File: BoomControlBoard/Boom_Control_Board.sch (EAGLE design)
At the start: 43 parts, among them J1 Servo Header, J2 FTDI Header, J7 455-1750-1-ND, U1 ATMEGA328P_TQFP, U2 3.3V/150mA, Y1 16MHz

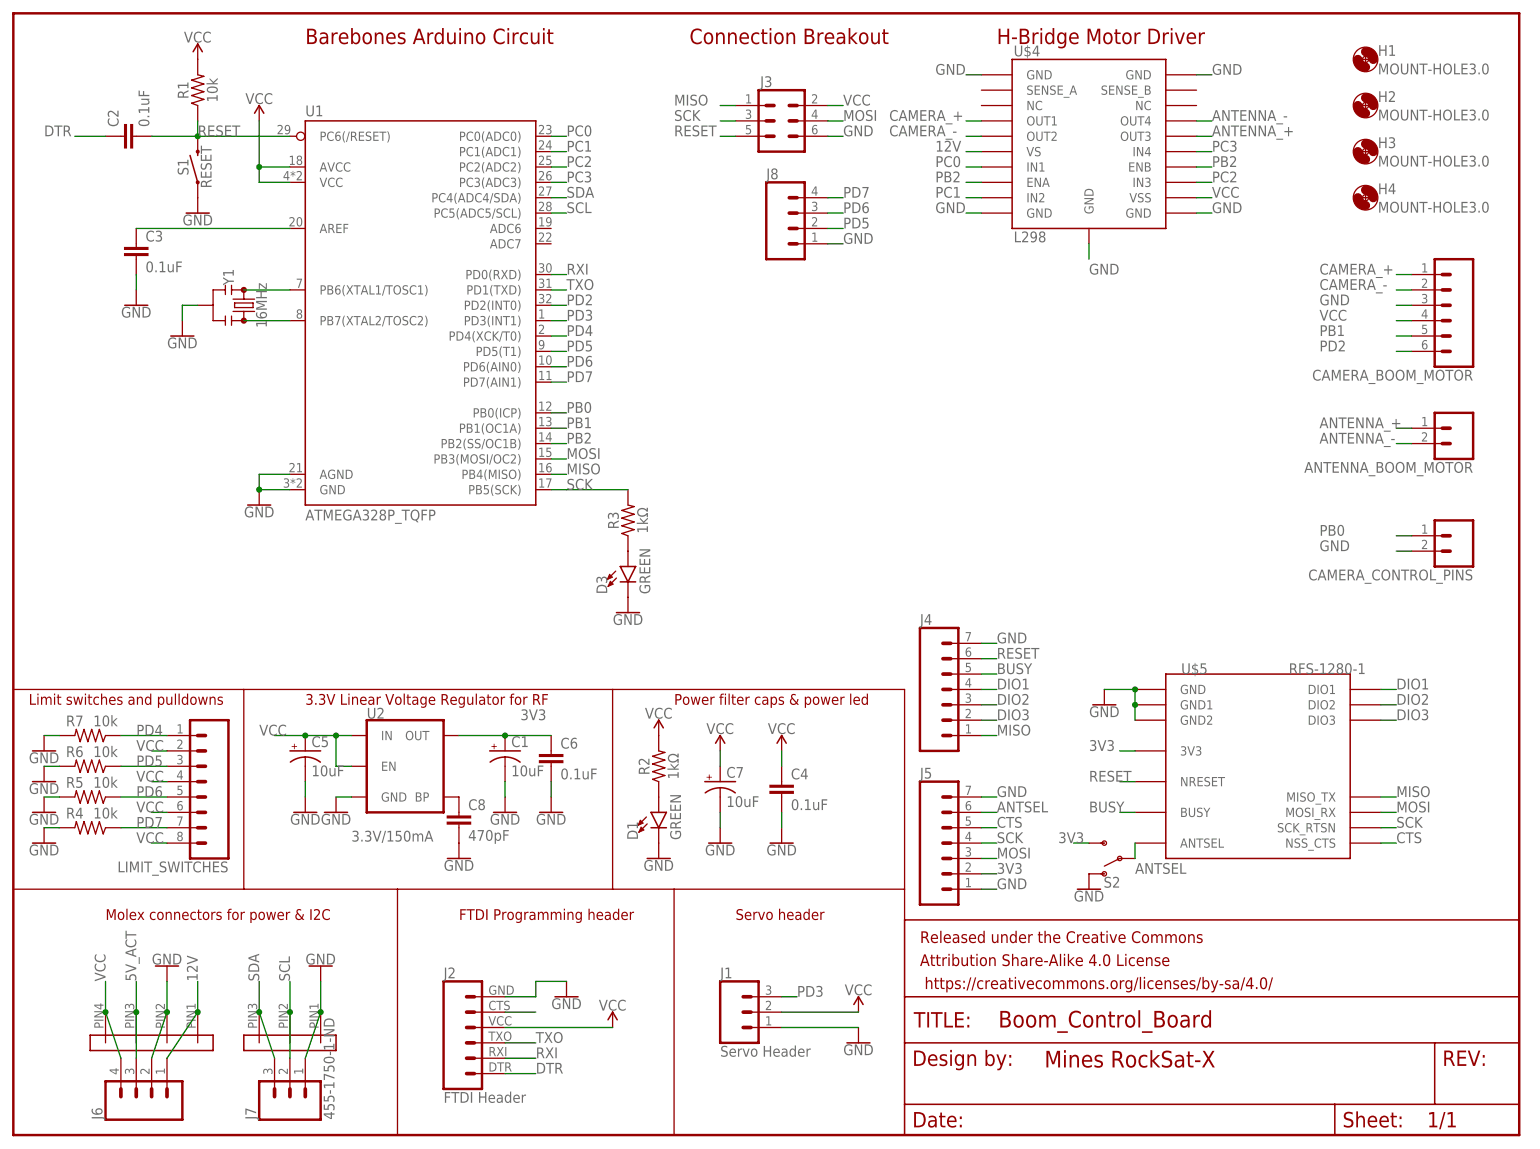
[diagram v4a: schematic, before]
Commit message: Lots of Labels added, GND connections added, component labels embiggened, traces rerouted.
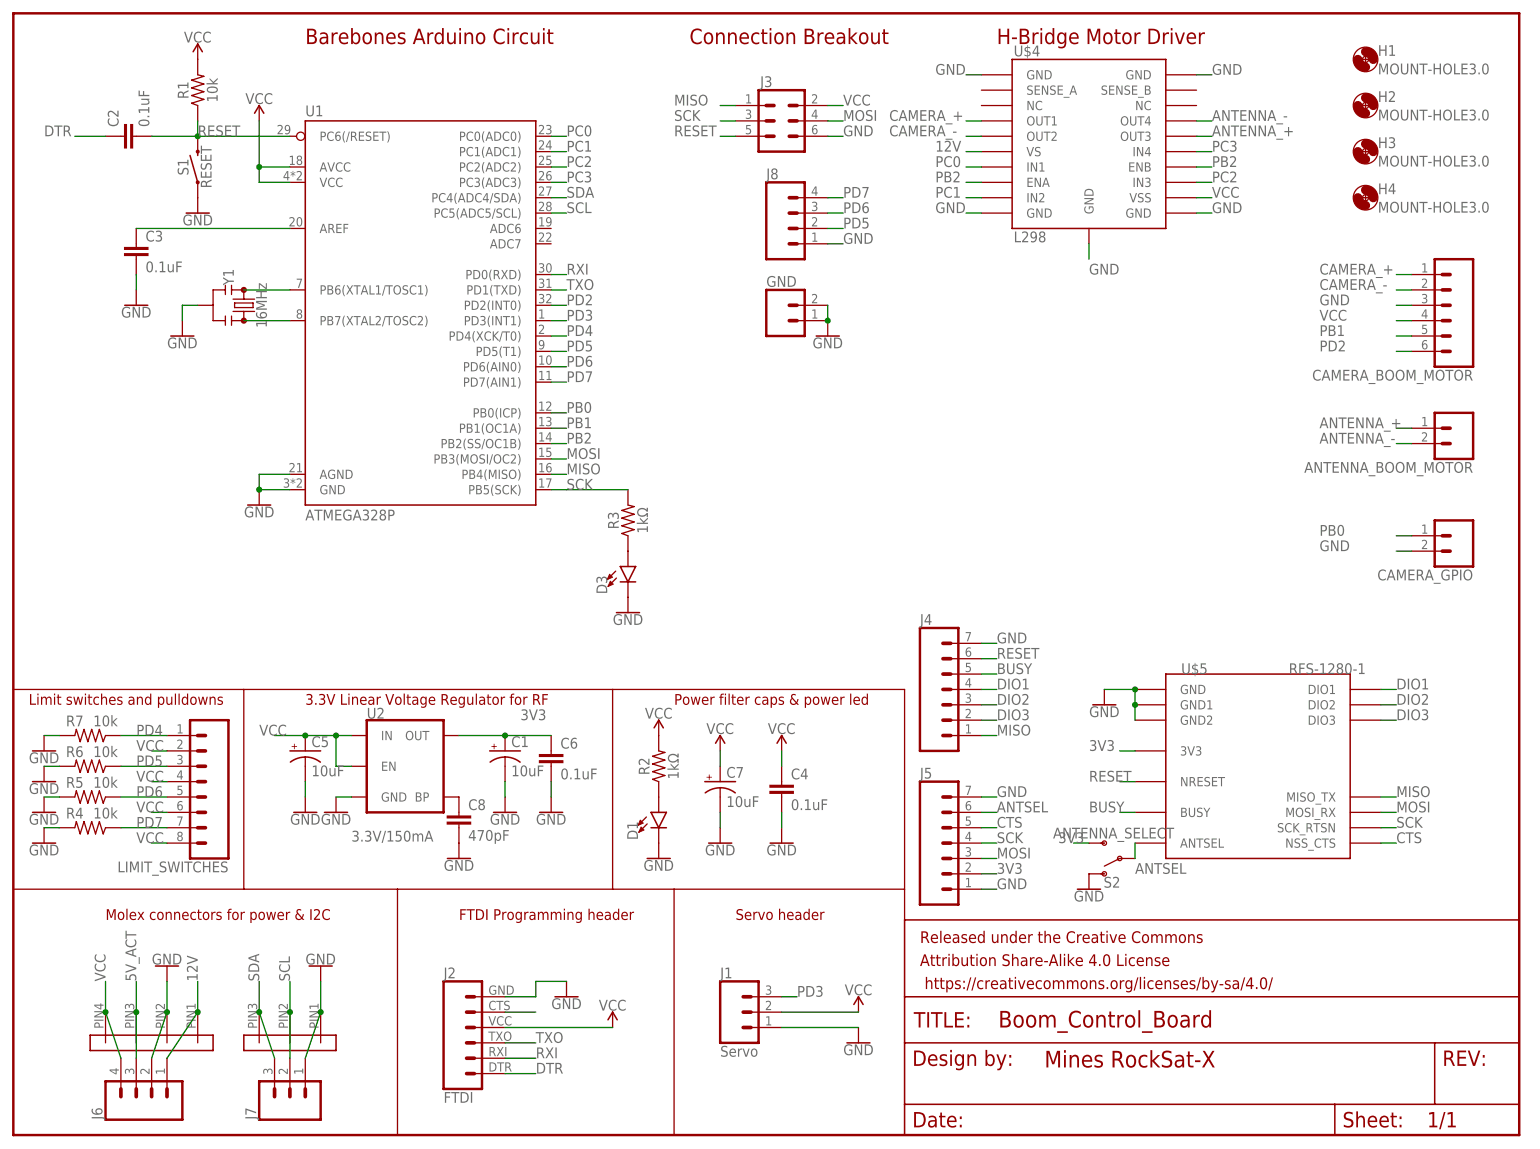
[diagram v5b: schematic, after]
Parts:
- added GND: (no value), SparkFun-Connectors:CONN_02LOCK_LONGPADS
- D1, D3: value GREEN -> (none)
- J1: value Servo Header -> Servo
- J2: value FTDI Header -> FTDI
- J7: value 455-1750-1-ND -> (none)
- S2: value (none) -> ANTENNA_SELECT
- U1: value ATMEGA328P_TQFP -> ATMEGA328P
- renumbered CAMERA_CONTROL_PINS to CAMERA_GPIO
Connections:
- net GND: now also GND.1, GND.2
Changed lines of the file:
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@@
 </classes>
 <parts>
-<part name="U1" library="SparkFun-IC-Microcontroller" deviceset="ATMEGA328P_TQFP" device="" value="ATMEGA328P_TQFP"/>
-<part name="J1" library="SparkFun-Connectors" deviceset="CONN_03" device="" value="Servo Header"/>
-<part name="J2" library="SparkFun-Connectors" deviceset="6_PIN_SERIAL_CABLE" device="PTH" value="FTDI Header"/>
+<part name="U1" library="SparkFun-IC-Microcontroller" deviceset="ATMEGA328P_TQFP" device="" value="ATMEGA328P"/>
+<part name="J1" library="SparkFun-Connectors" deviceset="CONN_03" device="" value="Servo"/>
+<part name="J2" library="SparkFun-Connectors" deviceset="6_PIN_SERIAL_CABLE" device="PTH" value="FTDI"/>
 <part name="C2" library="SparkFun-Capacitors" deviceset="2.2UF" device="-0805-25V-(+80/-20%)" value="0.1uF"/>
 <part name="C3" library="SparkFun-Capacitors" deviceset="2.2UF" device="-0805-25V-(+80/-20%)" value="0.1uF"/>
@@
 <part name="S1" library="SparkFun-Switches" deviceset="MOMENTARY-SWITCH-SPST" device="-SMD-5.2-REDUNDANT" value="RESET"/>
 <part name="GND13" library="SparkFun-PowerSymbols" deviceset="GND" device=""/>
-<part name="D1" library="SparkFun-LED" deviceset="LED-GREEN" device="1206" value="GREEN"/>
+<part name="D1" library="SparkFun-LED" deviceset="LED-GREEN" device="1206"/>
 <part name="GND1" library="SparkFun-PowerSymbols" deviceset="GND" device=""/>
 <part name="R3" library="SparkFun-Resistors" deviceset="RESISTOR" device="0805" value="1kΩ"/>
-<part name="D3" library="SparkFun-LED" deviceset="LED-GREEN" device="1206" value="GREEN"/>
+<part name="D3" library="SparkFun-LED" deviceset="LED-GREEN" device="1206"/>
 <part name="CAMERA_BOOM_MOTOR" library="SparkFun-Connectors" deviceset="CONN_06" device="LOCK_LONGPADS"/>
 <part name="ANTENNA_BOOM_MOTOR" library="SparkFun-Connectors" deviceset="CONN_02" device="LOCK_LONGPADS"/>
 <part name="LIMIT_SWITCHES" library="SparkFun-Connectors" deviceset="CONN_08" device="LOCK_LONGPADS"/>
-<part name="CAMERA_CONTROL_PINS" library="SparkFun-Connectors" deviceset="CONN_02" device="LOCK_LONGPADS"/>
+<part name="CAMERA_GPIO" library="SparkFun-Connectors" deviceset="CONN_02" device="LOCK_LONGPADS"/>
 <part name="R4" library="SparkFun-Resistors" deviceset="RESISTOR" device="0805" value="10k"/>
 <part name="R5" library="SparkFun-Resistors" deviceset="RESISTOR" device="0805" value="10k"/>
@@
 <part name="GND20" library="SparkFun-PowerSymbols" deviceset="GND" device=""/>
 <part name="GND21" library="SparkFun-PowerSymbols" deviceset="GND" device=""/>
-<part name="S2" library="SparkFun-Switches" deviceset="SWITCH-SPDT" device="-PTH-11.6X4.0MM"/>
+<part name="S2" library="SparkFun-Switches" deviceset="SWITCH-SPDT" device="-PTH-11.6X4.0MM" value="ANTENNA_SELECT"/>
 <part name="GND22" library="SparkFun-PowerSymbols" deviceset="GND" device=""/>
 <part name="C7" library="SparkFun-Capacitors" deviceset="10UF-POLAR" device="-EIA3216-16V-10%(TANT)" value="10uF"/>
@@
 <part name="U$5" library="PowerManagementParts" deviceset="RFS-1280-1" device=""/>
 <part name="J6" library="SparkFun-Connectors" deviceset="CONN_04" device="LOCK"/>
-<part name="J7" library="SparkFun-Connectors" deviceset="CONN_03" device="" value="455-1750-1-ND"/>
+<part name="J7" library="SparkFun-Connectors" deviceset="CONN_03" device=""/>
 <part name="J8" library="SparkFun-Connectors" deviceset="CONN_04" device="LOCK"/>
+<part name="GND" library="SparkFun-Connectors" deviceset="CONN_02" device="LOCK_LONGPADS"/>
+<part name="GND24" library="SparkFun-PowerSymbols" deviceset="GND" device=""/>
 </parts>
 <sheets>
@@
 <attribute name="NAME" x="35.56" y="45.212" size="1.778" layer="95" font="vector" rot="R180"/>
 </instance>
-<instance part="CAMERA_CONTROL_PINS" gate="G$1" x="238.76" y="99.06" smashed="yes" rot="R180">
+<instance part="CAMERA_GPIO" gate="G$1" x="238.76" y="99.06" smashed="yes" rot="R180">
 <attribute name="VALUE" x="241.3" y="103.886" size="1.778" layer="96" font="vector" rot="R180"/>
 <attribute name="NAME" x="241.3" y="93.472" size="1.778" layer="95" font="vector" rot="R180"/>
@@
 <attribute name="VALUE" x="124.46" y="142.494" size="1.778" layer="96" font="vector"/>
 <attribute name="NAME" x="124.46" y="157.988" size="1.778" layer="95" font="vector"/>
+</instance>
+<instance part="GND" gate="G$1" x="127" y="134.62" smashed="yes">
+<attribute name="VALUE" x="124.46" y="129.794" size="1.778" layer="96" font="vector"/>
+<attribute name="NAME" x="124.46" y="140.208" size="1.778" layer="95" font="vector"/>
+</instance>
+<instance part="GND24" gate="1" x="134.62" y="132.08" smashed="yes">
+<attribute name="VALUE" x="134.62" y="131.826" size="1.778" layer="96" align="top-center"/>
 </instance>
 </instances>
@@
 </segment>
 <segment>
-<pinref part="CAMERA_CONTROL_PINS" gate="G$1" pin="2"/>
+<pinref part="CAMERA_GPIO" gate="G$1" pin="2"/>
 <wire x1="231.14" y1="96.52" x2="228.6" y2="96.52" width="0.1524" layer="91"/>
 <label x="215.9" y="96.52" size="1.778" layer="95"/>
@@
 <label x="137.16" y="147.32" size="1.778" layer="95"/>
 </segment>
+<segment>
+<pinref part="GND" gate="G$1" pin="1"/>
+<pinref part="GND24" gate="1" pin="GND"/>
+<pinref part="GND" gate="G$1" pin="2"/>
+<wire x1="134.62" y1="137.16" x2="134.62" y2="134.62" width="0.1524" layer="91"/>
+<junction x="134.62" y="134.62"/>
+</segment>
 </net>
 <net name="DTR" class="0">
@@
 </segment>
 <segment>
-<pinref part="CAMERA_CONTROL_PINS" gate="G$1" pin="1"/>
+<pinref part="CAMERA_GPIO" gate="G$1" pin="1"/>
 <wire x1="231.14" y1="99.06" x2="228.6" y2="99.06" width="0.1524" layer="91"/>
 <label x="215.9" y="99.06" size="1.778" layer="95"/>

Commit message: Initial Rev2 for Boom and Exp. Control boards
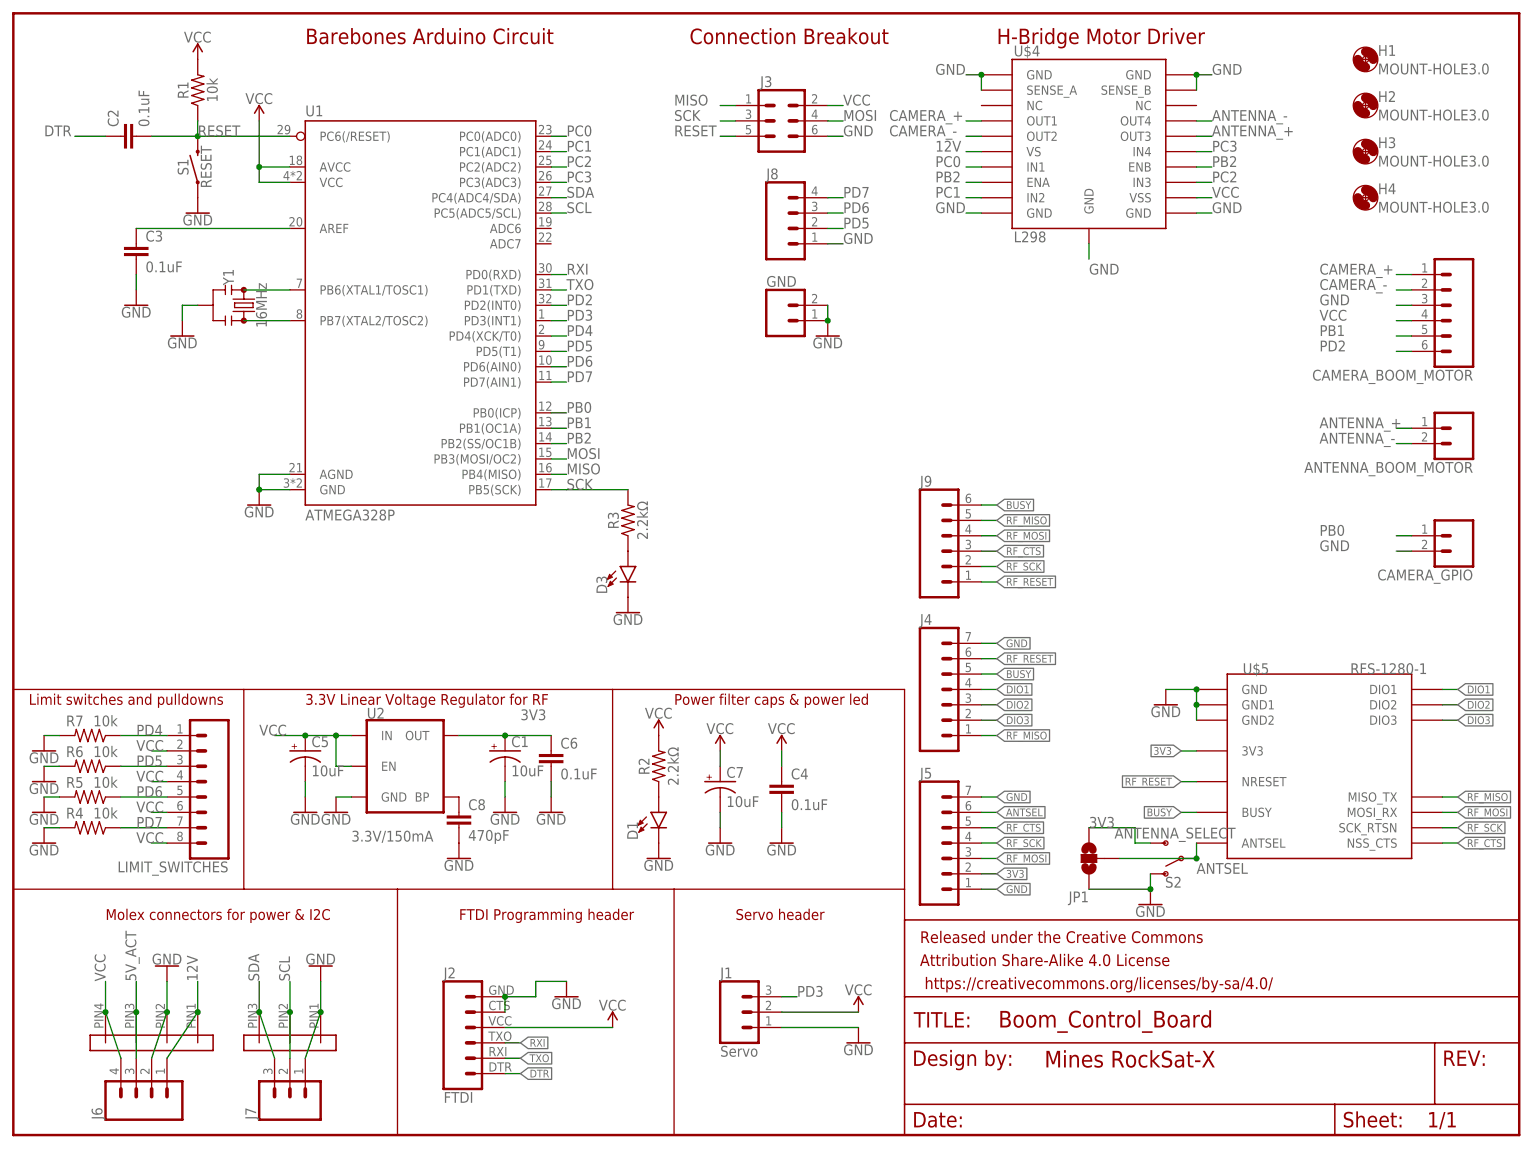
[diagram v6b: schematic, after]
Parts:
- added J9: (no value), SparkFun-Connectors:CONN_06LOCK
- added JP1: JUMPER-SMT_3_NO_NO_SILK, SparkFun-Jumpers:JUMPER-SMT_3_NO_NO_SILK
- R2, R3: value 1kΩ -> 2.2kΩ
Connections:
- removed net CTS: J5.5, U$5.NSS_CTS
- removed net N$6: J2.5
- new net RF_CTS: J5.5, J9.3, U$5.NSS_CTS
- new net RF_MISO: J4.1, J9.5, U$5.MISO_TX
- new net RF_MOSI: J5.3, J9.4, U$5.MOSI_RX
- new net RF_RESET: J4.6, J9.1, U$5.NRESET
- new net RF_SCK: J5.4, J9.2, U$5.SCK_RTSN
- net 3V3: now also JP1.3
- net ANTSEL: now also JP1.2
- net BUSY: now also J9.6
- net GND: now also J2.5, JP1.1, U$4.SENSE_A, U$4.SENSE_B
- net MISO: no longer J4.1, U$5.MISO_TX
- net MOSI: no longer J5.3, U$5.MOSI_RX
- net RESET: no longer J4.6, U$5.NRESET
- net RXI: now also J2.3; no longer J2.2
- net SCK: no longer J5.4, U$5.SCK_RTSN
- net TXO: now also J2.2; no longer J2.3
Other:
- moved on the sheet: S2, U$5
